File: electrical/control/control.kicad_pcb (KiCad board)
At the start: 2 copper layers, 33 x 48 mm, 42 parts, among them J1 USB4105-GF-A, J2 SWD, J3 TC2030-NL, J4 UART, J5 QWIIC, SW1 228EMSARGFR, U1 USBLC6-2P6, U2 LP5912-3.3DRV, U3 W25Q16JVUXIQ, U4 RP2040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

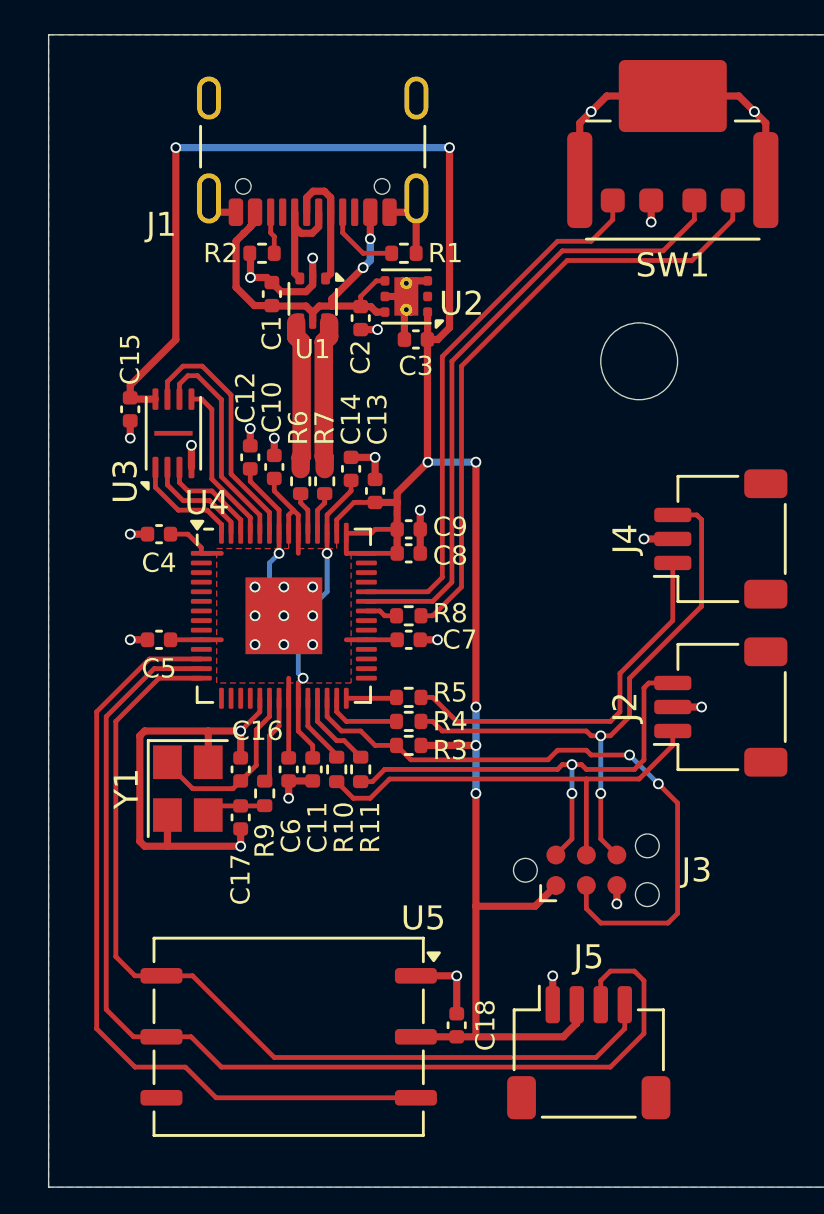
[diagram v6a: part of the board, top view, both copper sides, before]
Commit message: PCB cleanup and DRC fixes
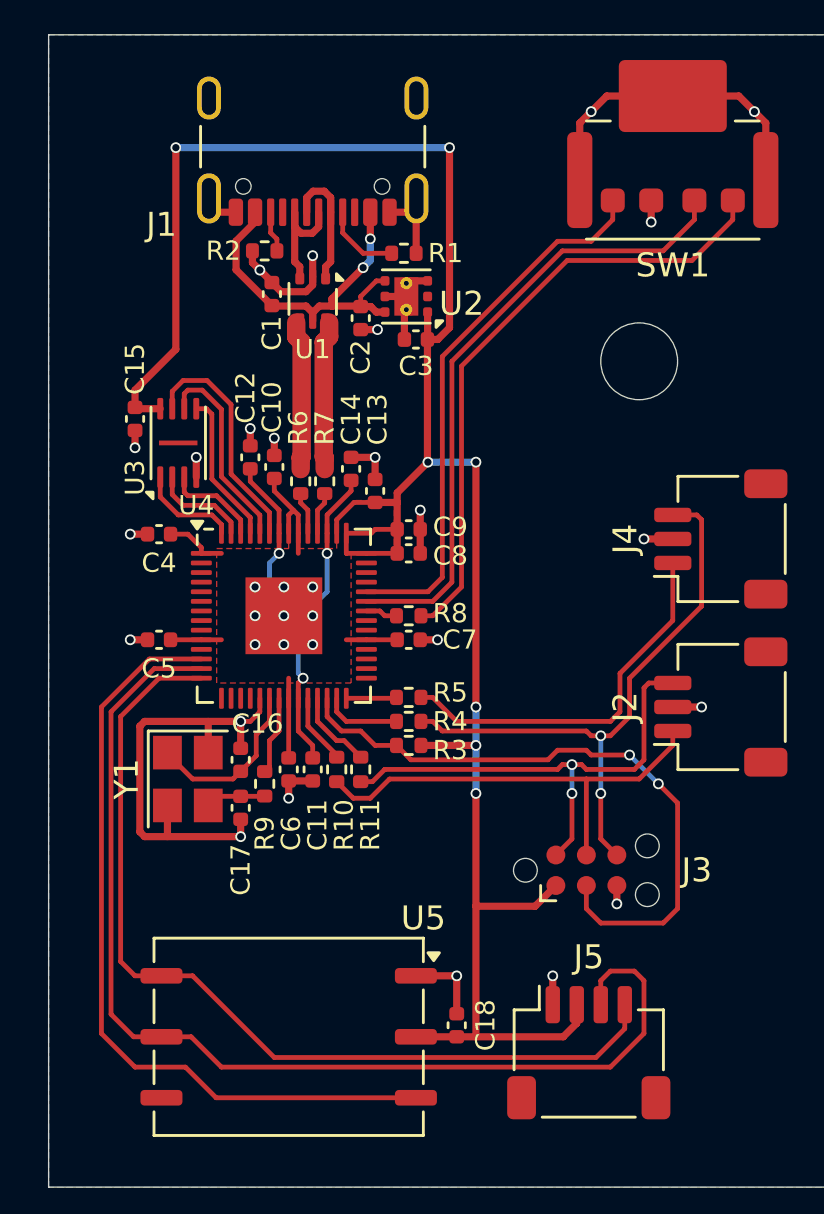
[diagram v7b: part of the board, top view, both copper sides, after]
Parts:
- moved U3 0.45 mm to (147.4, 85.0)
- moved C15 0.45 mm to (145.6, 84.0)
- moved Y1 0.40 mm to (147.8, 99.0)
- moved C16 0.40 mm to (150.0, 98.2)
- moved C17 0.40 mm to (150.0, 100.2)
- moved R9 0.40 mm to (151.0, 99.2)
- moved R2 0.15 mm to (151.0, 77.0)
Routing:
- net /QSPI_SD3: track 10.6 -> 9.80 mm
- net /QSPI_SCLK: track 9.16 -> 8.39 mm
- net GND: track 66.1 -> 65.6 mm

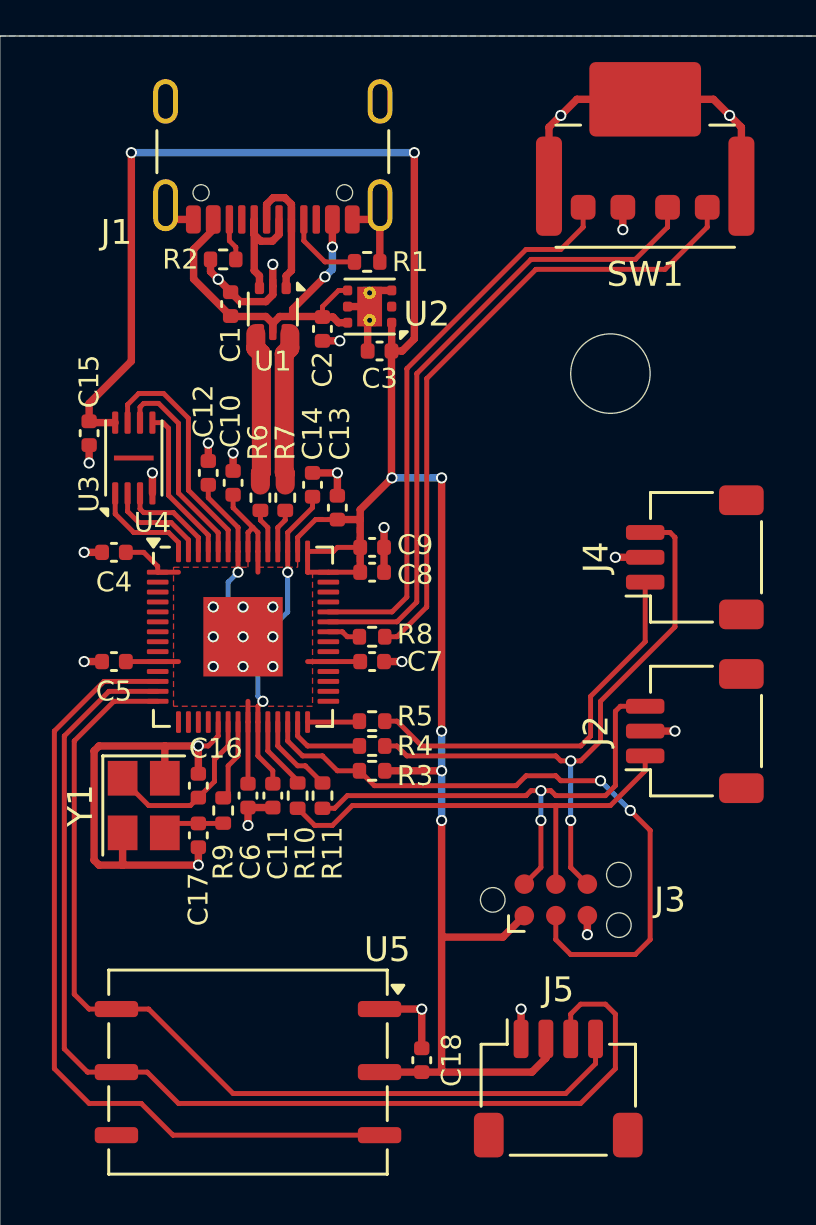
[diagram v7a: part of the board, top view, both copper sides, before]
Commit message: Adjust USB and power routing
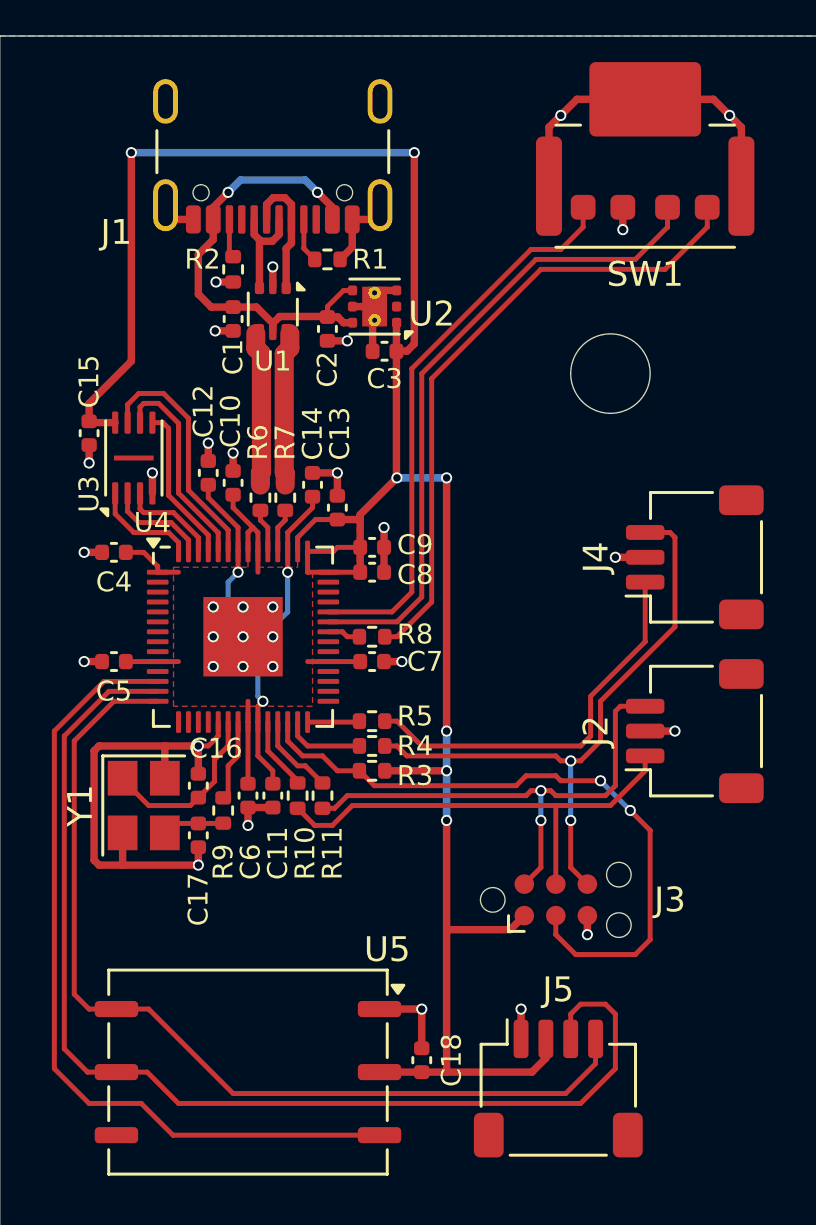
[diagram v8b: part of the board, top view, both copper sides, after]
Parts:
- moved R1 1.60 mm to (155.2, 77.0)
- moved C1 0.61 mm to (151.4, 79.4), turned to -90 degrees
- moved R2 0.57 mm to (151.4, 77.4), turned to -90 degrees
- moved C3 0.20 mm to (157.5, 80.7)
- moved C2 0.20 mm to (155.2, 79.8)
- moved U2 0.20 mm to (157.1, 78.9)
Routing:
- net GND: track 65.6 -> 62.5 mm, vias 32 -> 33
- net VBUS: track 16.5 -> 18.9 mm
- net Net-(J1-CC1): track 3.25 -> 1.79 mm
- net Net-(J1-D+-PadA6): track 5.29 -> 4.38 mm
